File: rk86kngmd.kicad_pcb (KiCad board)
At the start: 2 copper layers, 226.2 x 62.5 mm, 39 parts, among them P1 GND, P10 TR00, P11 WPRT, P12 RD_DATA, P13 SIDE, P14 READY, P2 +5V, P3 IP, P4 DISC_A, P5 DISC_B, P6 DIR, P7 STEP, P8 WR_DATA, P9 WR_GATE, X1 ОНп-КС-23

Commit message: .
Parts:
- removed P1: GND, Pin_Headers:Pin_Header_Straight_1x01
- removed P10: TR00, Pin_Headers:Pin_Header_Straight_1x01
- removed P11: WPRT, Pin_Headers:Pin_Header_Straight_1x01
- removed P12: RD_DATA, Pin_Headers:Pin_Header_Straight_1x01
- removed P13: SIDE, Pin_Headers:Pin_Header_Straight_1x01
- removed P14: READY, Pin_Headers:Pin_Header_Straight_1x01
- removed P2: +5V, Pin_Headers:Pin_Header_Straight_1x01
- removed P3: IP, Pin_Headers:Pin_Header_Straight_1x01
- removed P4: DISC_A, Pin_Headers:Pin_Header_Straight_1x01
- removed P5: DISC_B, Pin_Headers:Pin_Header_Straight_1x01
- removed P6: DIR, Pin_Headers:Pin_Header_Straight_1x01
- removed P7: STEP, Pin_Headers:Pin_Header_Straight_1x01
- removed P8: WR_DATA, Pin_Headers:Pin_Header_Straight_1x01
- removed P9: WR_GATE, Pin_Headers:Pin_Header_Straight_1x01
- added C2: 0.1, Capacitor_THT:C_Disc_D6.0mm_W2.5mm_P5.00mm, F.Cu at (56.2, 106.2)
- added C3: 0.1, Capacitor_THT:C_Disc_D6.0mm_W2.5mm_P5.00mm, F.Cu at (96.8, 80.8)
- added D2: 2N4148, Diode_THT:D_A-405_P2.54mm_Vertical_AnodeUp, F.Cu at (53.5, 120.0)
- added DD1: К580ВВ55, rk86kngmd:DIP40-2.5mm, F.Cu at (86.5, 59.5)
- added J1: Conn_02x17_Odd_Even, Connector_IDC:IDC-Header_2x17_P2.54mm_Vertical, F.Cu at (46.4, 53.9)
- added J2: FD power, rk86kngmd:171826-4, F.Cu at (49.9, 104.7)
- added R8: 1K, Resistor_THT:R_Axial_DIN0207_L6.3mm_D2.5mm_P2.54mm_Vertical, F.Cu at (45.9, 117.4)
- C1: footprint Capacitors_ThroughHole:C_Disc_D6_P5 -> Capacitor_THT:C_Disc_D6.0mm_W2.5mm_P5.00mm
- D1: value К580ВВ55 -> 2N4148; footprint rk86kngmd:DIP40-2.5mm -> Diode_THT:D_A-405_P2.54mm_Vertical_AnodeUp
- DD10: value К555ИД4 -> 74LS155; footprint DIP16-2.5mm -> Package_SO:SOIC-16_3.9x9.9mm_P1.27mm; moved to B.Cu
- DD11, DD12: value К555ТМ2 -> 74LS74; footprint rk86ngmd:DIP14-2.5mm -> Package_SO:SOIC-14_3.9x8.7mm_P1.27mm
- DD13: value К555ЛА3 -> 74LS00; footprint rk86ngmd:DIP14-2.5mm -> Package_SO:SOIC-14_3.9x8.7mm_P1.27mm
- DD14: value К555ЛН1 -> 74LS04; footprint rk86ngmd:DIP14-2.5mm -> Package_SO:SOIC-14_3.9x8.7mm_P1.27mm
- DD15: value К555ЛИ1 -> 74LS08; footprint rk86ngmd:DIP14-2.5mm -> Package_SO:SOIC-14_3.9x8.7mm_P1.27mm
- DD16: value К555ЛЛ1 -> 74LS32; footprint rk86ngmd:DIP14-2.5mm -> Package_SO:SOIC-14_3.9x8.7mm_P1.27mm
- DD17: value К555ЛЕ1 -> 74LS02; footprint DIP14-2.5mm -> Package_SO:SOIC-14_3.9x8.7mm_P1.27mm
- DD2: value К555ИР13 -> К155ИР13; footprint DIP24-2.5mm -> rk86kngmd:DIP24-2.5mm
- DD3: value К555ИР23 -> 74LS374; footprint DIP20-2.5mm -> Package_SO:SOIC-20W_7.5x12.8mm_P1.27mm
- DD4: value 2716 -> 27C64; footprint rk86ngmd:DIP24-2.5mm -> Package_DIP:DIP-28_W15.24mm_Socket
- DD6: value К555ИР22 -> 74LS373; footprint rk86ngmd:DIP20-2.5mm -> Package_SO:SOIC-20W_7.5x12.8mm_P1.27mm
- DD7, DD8: value К555ИЕ5 -> 74LS93; footprint rk86ngmd:DIP14-2.5mm -> Package_SO:SOIC-14_3.9x8.7mm_P1.27mm; moved to B.Cu
- DD9: value К555ИЕ7 -> 74LS193; footprint rk86ngmd:DIP16-2.5mm -> Package_SO:SOIC-16_3.9x9.9mm_P1.27mm; moved to B.Cu
- R1, R2, R3, R4, R5, R7: footprint rk86ngmd:Resistor_Vertical_RM2_5mm -> Resistor_THT:R_Axial_DIN0207_L6.3mm_D2.5mm_P2.54mm_Vertical
- R6: footprint Resistor_Vertical_RM2_5mm -> Resistor_THT:R_Axial_DIN0207_L6.3mm_D2.5mm_P2.54mm_Vertical
- X1: footprint rk86ngmd:ОНп-КС-23 -> rk86kngmd:ОНп-КС-23
- moved DD7 153.7 mm to (112.0, 114.9), turned to 0 degrees
- moved DD8 152.6 mm to (112.4, 94.6), turned to 0 degrees
- moved DD13 132.9 mm to (108.3, 94.6), turned to 0 degrees
- moved DD9 122.3 mm to (120.3, 78.3), turned to 0 degrees
- moved DD15 121.2 mm to (123.1, 114.9), turned to 0 degrees
- moved DD10 114.0 mm to (104.7, 78.2), turned to 0 degrees
- moved DD14 111.8 mm to (105.8, 77.8), turned to 0 degrees
- moved DD2 105.8 mm to (61.6, 97.6), turned to 180 degrees
- moved R1 98.0 mm to (109.2, 104.7), turned to 0 degrees
- moved DD17 94.6 mm to (123.0, 77.6), turned to 0 degrees
- moved DD11 94.5 mm to (123.1, 94.6), turned to 0 degrees
- moved C1 85.8 mm to (118.9, 104.7), turned to 0 degrees
- moved DD12 81.9 mm to (123.1, 60.0), turned to 0 degrees
- moved D1 72.1 mm to (49.9, 120.0), turned to 90 degrees
- moved DD3 58.0 mm to (85.5, 78.3)
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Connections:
- D1 pad 1: Net-(D1-Pad1) -> /CS1
- D1 pad 2: Net-(D1-Pad2) -> /CS12
- DD16 pad 8: Net-(D1-Pad6) -> Net-(DD1-Pad6)
- DD2 pad 15: Net-(D1-Pad40) -> Net-(DD1-Pad40)
- DD2 pad 17: Net-(D1-Pad39) -> Net-(DD1-Pad39)
- DD2 pad 19: Net-(D1-Pad38) -> Net-(DD1-Pad38)
- DD2 pad 21: Net-(D1-Pad37) -> Net-(DD1-Pad37)
- DD2 pad 3: Net-(D1-Pad4) -> Net-(DD1-Pad4)
- DD2 pad 5: Net-(D1-Pad3) -> Net-(DD1-Pad3)
- DD2 pad 7: Net-(D1-Pad2) -> Net-(DD1-Pad2)
- DD2 pad 9: Net-(D1-Pad1) -> Net-(DD1-Pad1)
- DD4 pad 1: /A7 -> +5V
- DD4 pad 10: /D1 -> /A0
- DD4 pad 11: /D2 -> /D0
- DD4 pad 12: GND -> /D1
- DD4 pad 13: /D3 -> /D2
- DD4 pad 14: /D4 -> GND
- DD4 pad 15: /D5 -> /D3
- DD4 pad 16: /D6 -> /D4
- DD4 pad 17: /D7 -> /D5
- DD4 pad 18: /CS1 -> /D6
- DD4 pad 19: /A10 -> /D7
- DD4 pad 2: /A6 -> GND
- DD4 pad 20: /RD -> /CS12
- DD4 pad 21: +5V -> /A10
- DD4 pad 22: /A9 -> /RD
- DD4 pad 23: /A8 -> /A11
- DD4 pad 24: +5V -> /A9
- DD4 pad 3: /A5 -> /A7
- DD4 pad 4: /A4 -> /A6
- DD4 pad 5: /A3 -> /A5
- DD4 pad 6: /A2 -> /A4
- DD4 pad 7: /A1 -> /A3
- DD4 pad 8: /A0 -> /A2
- DD4 pad 9: /D0 -> /A1
- X1 pad B11: Net-(X1-PadB11) -> +12V
- X1 pad B23: Net-(X1-PadB23) -> /A11
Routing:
- net GND: track 608.9 -> 0.00 mm, vias 10 -> 0
- net +5V: track 574.7 -> 0.00 mm, vias 6 -> 0
- net Net-(DD10-Pad1): track 372.7 -> 0.00 mm, vias 16 -> 0
- net Net-(DD15-Pad11): track 247.4 -> 0.00 mm, vias 8 -> 0
- net RD_DATA: track 247.0 -> 0.00 mm, vias 13 -> 0
- net /RD: track 238.5 -> 0.00 mm, vias 8 -> 0
- net /WRDATA: track 219.4 -> 0.00 mm, vias 8 -> 0
- net /OSC: track 218.3 -> 0.00 mm, vias 4 -> 0
- net /WRGATE: track 202.8 -> 0.00 mm, vias 9 -> 0
- net Net-(DD12-Pad13): track 200.3 -> 0.00 mm, vias 3 -> 0
- net Net-(DD16-Pad3): track 175.5 -> 0.00 mm, vias 5 -> 0
- net /A2: track 175.1 -> 0.00 mm, vias 4 -> 0
- net /WR: track 169.8 -> 0.00 mm, vias 5 -> 0
- net Net-(DD11-Pad3): track 159.7 -> 0.00 mm, vias 5 -> 0
- net /D4: track 146.2 -> 0.00 mm, vias 6 -> 0
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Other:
- board size 226.2 x 62.5 mm -> 86.9 x 84.7 mm
- board text added: "+12"
- board text added: "+5"
- board text added: "Gnd"
- board text added: "RK86 FD Controller"
- board text added: "©2020 SDS"
- board text removed: "2016 tnt23"

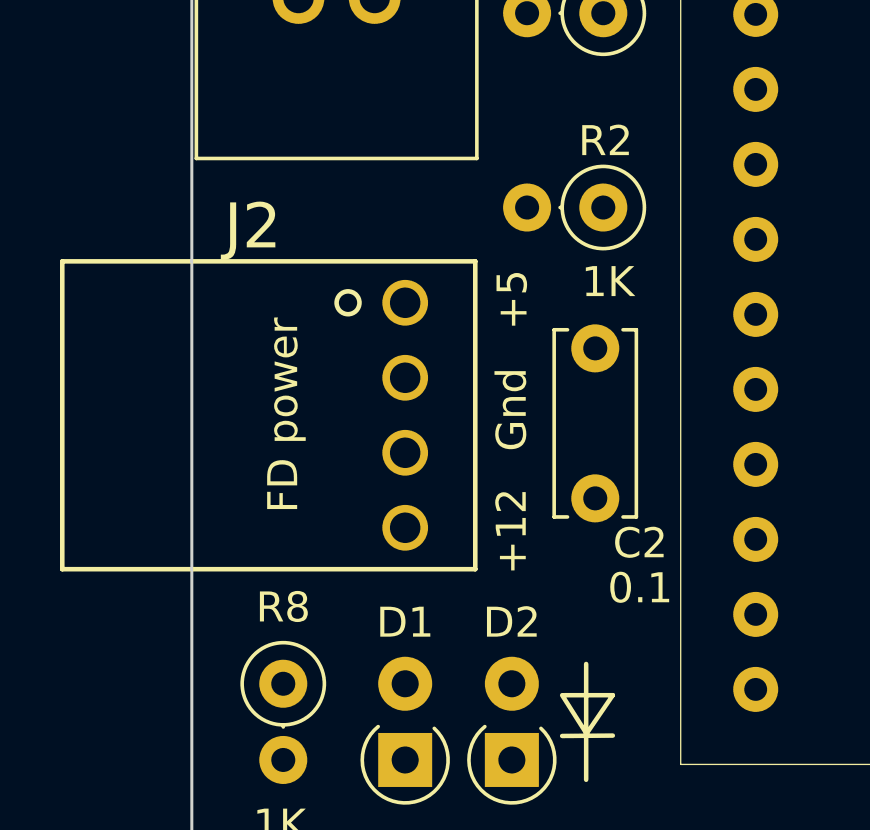
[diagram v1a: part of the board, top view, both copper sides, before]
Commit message: Updated libraries
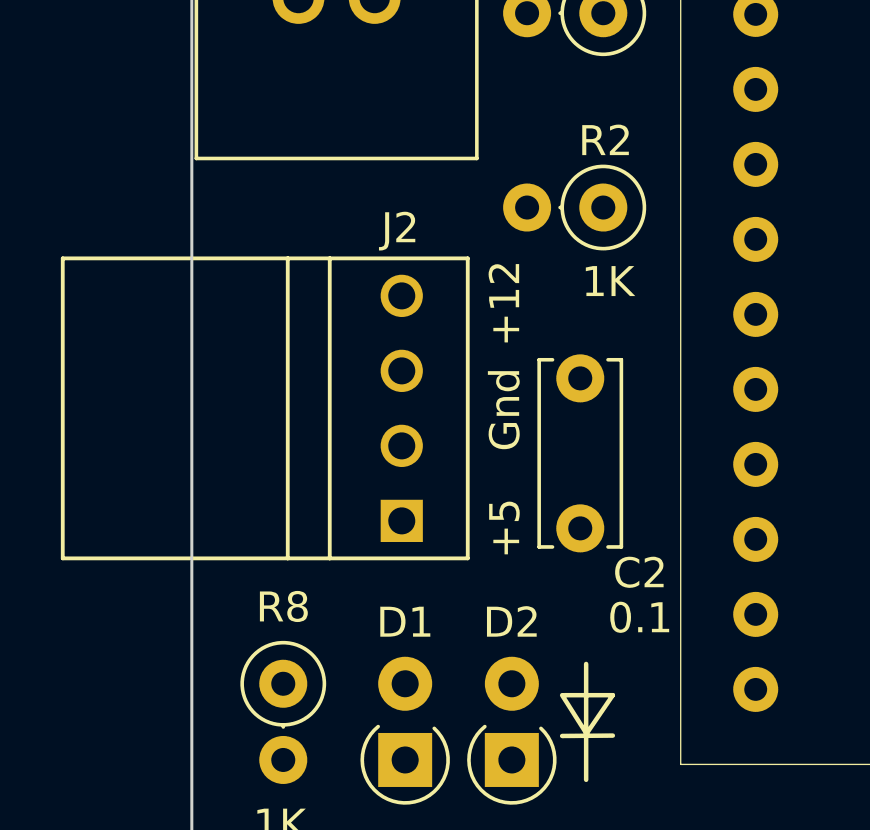
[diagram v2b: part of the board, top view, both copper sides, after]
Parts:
- J2: footprint rk86kngmd:171826-4 -> rk86kngmd:TE_171826-4
- moved C2 6.02 mm to (55.8, 112.2), turned to 90 degrees
- moved J2 5.84 mm to (45.2, 108.2)
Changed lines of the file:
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@@
     (add_net GND)
+  )
+  (module rk86kngmd:TE_171826-4 (layer F.Cu)
+    (at 45.25 108.25 270)
+    (fp_text reference J2 (at -6 -4.5 180) (layer F.SilkS)
+      (effects (font (size 1 1) (thickness 0.15)))
+    )
+    (fp_text value "FD power" (at 1.991485 7.991205 90) (layer F.Fab)
+      (effects (font (size 1.003283 1.003283) (thickness 0.015)))
+    )
+    (fp_line (start -5 -2.15) (end 5 -2.15) (layer F.SilkS) (width 0.127))
+    (fp_line (start -5 -0.75) (end 5 -0.75) (layer F.SilkS) (width 0.127))
+    (fp_line (start 5 6.75) (end -5 6.75) (layer F.Fab) (width 0.127))
+    (fp_line (start -5 -6.75) (end 5 -6.75) (layer F.Fab) (width 0.127))
+    (fp_line (start -5 6.75) (end -5 -6.75) (layer F.Fab) (width 0.127))
+    (fp_line (start 5 6.75) (end 5 -6.75) (layer F.Fab) (width 0.127))
+    (fp_line (start -5.25 7) (end -5.25 -7) (layer F.CrtYd) (width 0.05))
+    (fp_line (start 5.25 7) (end -5.25 7) (layer F.CrtYd) (width 0.05))
+    (fp_line (start 5.25 -7) (end 5.25 7) (layer F.CrtYd) (width 0.05))
+    (fp_line (start -5.25 -7) (end 5.25 -7) (layer F.CrtYd) (width 0.05))
+    (fp_line (start -5 -2.15) (end -5 -6.75) (layer F.SilkS) (width 0.127))
+    (fp_line (start -5 -0.75) (end -5 -2.15) (layer F.SilkS) (width 0.127))
+    (fp_line (start -5 6.75) (end -5 -0.75) (layer F.SilkS) (width 0.127))
+    (fp_line (start 5 6.75) (end -5 6.75) (layer F.SilkS) (width 0.127))
+    (fp_line (start 5 -0.75) (end 5 6.75) (layer F.SilkS) (width 0.127))
+    (fp_line (start 5 -2.15) (end 5 -0.75) (layer F.SilkS) (width 0.127))
+    (fp_line (start 5 -6.75) (end 5 -2.15) (layer F.SilkS) (width 0.127))
+    (fp_line (start -5 -6.75) (end 5 -6.75) (layer F.SilkS) (width 0.127))
+    (pad 1 thru_hole rect (at 3.75 -4.55 270) (size 1.408 1.408) (drill 0.9) (layers *.Cu *.Mask)
+      (net 21 +5V))
+    (pad 2 thru_hole circle (at 1.25 -4.55 270) (size 1.408 1.408) (drill 0.9) (layers *.Cu *.Mask)
+      (net 1 GND))
+    (pad 3 thru_hole circle (at -1.25 -4.55 270) (size 1.408 1.408) (drill 0.9) (layers *.Cu *.Mask)
+      (net 1 GND))
+    (pad 4 thru_hole circle (at -3.75 -4.55 270) (size 1.408 1.408) (drill 0.9) (layers *.Cu *.Mask)
+      (net 163 +12V))
   )
   (module Capacitor_THT:C_Disc_D6.0mm_W2.5mm_P5.00mm (layer F.Cu)
@@
   )
   (module Capacitor_THT:C_Disc_D6.0mm_W2.5mm_P5.00mm (layer F.Cu)
-    (at 56.25 106.25 270)
+    (at 55.75 112.25 90)
     (descr "C, Disc series, Radial, pin pitch=5.00mm, , diameter*width=6*2.5mm^2, Capacitor, http://cdn-reichelt.de/documents/datenblatt/B300/DS_KERKO_TC.pdf")
     (tags "C Disc series Radial pin pitch 5.00mm  diameter 6mm width 2.5mm Capacitor")
-    (fp_text reference C2 (at 6.5 -1.5 180) (layer F.SilkS)
-      (effects (font (size 1 1) (thickness 0.15)))
-    )
-    (fp_text value 0.1 (at 8 -1.5) (layer F.SilkS)
+    (fp_text reference C2 (at -1.5 2 180) (layer F.SilkS)
+      (effects (font (size 1 1) (thickness 0.15)))
+    )
+    (fp_text value 0.1 (at -3 2) (layer F.SilkS)
       (effects (font (size 1 1) (thickness 0.15)))
     )
@@
     (fp_line (start -0.5 1.25) (end 5.5 1.25) (layer F.Fab) (width 0.1))
     (fp_line (start -0.5 -1.25) (end -0.5 1.25) (layer F.Fab) (width 0.1))
-    (pad 2 thru_hole circle (at 5 0 270) (size 1.6 1.6) (drill 0.8) (layers *.Cu *.Mask)
-      (net 1 GND))
-    (pad 1 thru_hole circle (at 0 0 270) (size 1.6 1.6) (drill 0.8) (layers *.Cu *.Mask)
+    (pad 2 thru_hole circle (at 5 0 90) (size 1.6 1.6) (drill 0.8) (layers *.Cu *.Mask)
+      (net 1 GND))
+    (pad 1 thru_hole circle (at 0 0 90) (size 1.6 1.6) (drill 0.8) (layers *.Cu *.Mask)
       (net 21 +5V))
     (model ${KISYS3DMOD}/Capacitor_THT.3dshapes/C_Disc_D6.0mm_W2.5mm_P5.00mm.wrl
@@
       (rotate (xyz 0 0 0))
     )
-  )
-  (module rk86kngmd:171826-4 (layer F.Cu)
-    (at 49.914 104.73 270)
-    (fp_text reference J2 (at -2.54 5.08 180) (layer F.SilkS)
-      (effects (font (size 1.5 1.5) (thickness 0.15)))
-    )
-    (fp_text value "FD power" (at 3.75 4.064 90) (layer F.SilkS)
-      (effects (font (size 1 1) (thickness 0.15)))
-    )
-    (fp_circle (center 0 1.905) (end 0.381 1.905) (layer F.Fab) (width 0.1524))
-    (fp_circle (center 0 1.905) (end 0.381 1.905) (layer B.SilkS) (width 0.1524))
-    (fp_circle (center 0 1.905) (end 0.381 1.905) (layer F.SilkS) (width 0.1524))
-    (fp_line (start 9.0078 -2.4638) (end -1.5078 -2.4638) (layer F.CrtYd) (width 0.1524))
-    (fp_line (start 9.0078 11.557) (end 9.0078 -2.4638) (layer F.CrtYd) (width 0.1524))
-    (fp_line (start -1.5078 11.557) (end 9.0078 11.557) (layer F.CrtYd) (width 0.1524))
-    (fp_line (start -1.5078 -2.4638) (end -1.5078 11.557) (layer F.CrtYd) (width 0.1524))
-    (fp_line (start -1.2538 -2.2098) (end -1.2538 11.303) (layer F.Fab) (width 0.1524))
-    (fp_line (start 8.7538 -2.2098) (end -1.2538 -2.2098) (layer F.Fab) (width 0.1524))
-    (fp_line (start 8.7538 11.303) (end 8.7538 -2.2098) (layer F.Fab) (width 0.1524))
-    (fp_line (start -1.2538 11.303) (end 8.7538 11.303) (layer F.Fab) (width 0.1524))
-    (fp_line (start -1.3808 -2.3368) (end -1.3808 11.43) (layer F.SilkS) (width 0.1524))
-    (fp_line (start 8.8808 -2.3368) (end -1.3808 -2.3368) (layer F.SilkS) (width 0.1524))
-    (fp_line (start 8.8808 11.43) (end 8.8808 -2.3368) (layer F.SilkS) (width 0.1524))
-    (fp_line (start -1.3808 11.43) (end 8.8808 11.43) (layer F.SilkS) (width 0.1524))
-    (fp_text user "Copyright 2016 Accelerated Designs. All rights reserved." (at 0 0 90) (layer Cmts.User)
-      (effects (font (size 0.127 0.127) (thickness 0.002)))
-    )
-    (pad 4 thru_hole circle (at 7.5 0 270) (size 1.524 1.524) (drill 1.016) (layers *.Cu *.Mask)
-      (net 163 +12V))
-    (pad 3 thru_hole circle (at 5 0 270) (size 1.524 1.524) (drill 1.016) (layers *.Cu *.Mask)
-      (net 1 GND))
-    (pad 2 thru_hole circle (at 2.5 0 270) (size 1.524 1.524) (drill 1.016) (layers *.Cu *.Mask)
-      (net 1 GND))
-    (pad 1 thru_hole circle (at 0 0 270) (size 1.524 1.524) (drill 1.016) (layers *.Cu *.Mask)
-      (net 21 +5V))
   )
   (module rk86kngmd:ОНп-КС-23 (layer F.Cu)
@@
     (effects (font (size 2 2) (thickness 0.3)) (justify mirror))
   )
-  (gr_text Gnd (at 53.47 108.286 90) (layer F.SilkS)
+  (gr_text Gnd (at 53.25 108.286 90) (layer F.SilkS)
     (effects (font (size 1 1) (thickness 0.15)))
   )
-  (gr_text +5 (at 53.4954 104.6284 90) (layer F.SilkS)
+  (gr_text +5 (at 53.25 112.25 90) (layer F.SilkS)
     (effects (font (size 1 1) (thickness 0.15)))
   )
-  (gr_text +12 (at 53.47 112.35 90) (layer F.SilkS)
+  (gr_text +12 (at 53.25 104.75 90) (layer F.SilkS)
     (effects (font (size 1 1) (thickness 0.15)))
   )

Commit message: board routed
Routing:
- net GND: track 0.00 -> 498.6 mm, vias 0 -> 4
- net +5V: track 0.00 -> 427.5 mm, vias 0 -> 5
- net Net-(DD10-Pad1): track 0.00 -> 231.3 mm, vias 0 -> 3
- net /WR: track 0.00 -> 145.1 mm, vias 0 -> 1
- net /RD: track 0.00 -> 118.1 mm, vias 0 -> 3
- net /D2: track 0.00 -> 117.9 mm, vias 0 -> 1
- net /D1: track 0.00 -> 116.4 mm, vias 0 -> 1
- net Net-(DD13-Pad1): track 0.00 -> 114.1 mm, vias 0 -> 3
- net /D0: track 0.00 -> 109.6 mm, vias 0 -> 3
- net Net-(DD11-Pad3): track 0.00 -> 108.8 mm, vias 0 -> 6
- net Net-(DD17-Pad1): track 0.00 -> 105.4 mm, vias 0 -> 1
- net TR00: track 0.00 -> 103.7 mm
- net READY: track 0.00 -> 103.5 mm
- net /D7: track 0.00 -> 102.0 mm, vias 0 -> 1
- net Net-(DD12-Pad5): track 0.00 -> 101.1 mm, vias 0 -> 1
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- added copper zone on B.Cu, net GND
- added copper zone on F.Cu, net GND

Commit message: Switched to SMD components
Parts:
- C1: footprint Capacitor_THT:C_Disc_D6.0mm_W2.5mm_P5.00mm -> Capacitor_SMD:C_1206_3216Metric_Pad1.42x1.75mm_HandSolder
- C2, C3: value 0.1 -> 0μ1; footprint Capacitor_THT:C_Disc_D6.0mm_W2.5mm_P5.00mm -> Capacitor_SMD:C_1206_3216Metric_Pad1.42x1.75mm_HandSolder
- D1, D2: footprint Diode_THT:D_A-405_P2.54mm_Vertical_AnodeUp -> Diode_SMD:D_1206_3216Metric_Pad1.42x1.75mm_HandSolder
- R1, R2, R3, R4, R5, R6, R7, R8: footprint Resistor_THT:R_Axial_DIN0207_L6.3mm_D2.5mm_P2.54mm_Vertical -> Resistor_SMD:R_1206_3216Metric_Pad1.42x1.75mm_HandSolder
- moved R2 2.43 mm to (55.8, 99.2)
- moved C3 1.71 mm to (97.0, 79.0)
- moved D1 1.49 mm to (49.8, 118.5)
- moved D2 1.48 mm to (53.5, 118.5)
- moved C2 1.20 mm to (55.8, 111.0)
- moved R8 1.07 mm to (46.0, 118.5)
- moved R4 0.81 mm to (55.8, 82.9)
- moved R6 0.81 mm to (55.8, 87.0)
- moved R5 0.77 mm to (55.8, 95.1)
- moved R7 0.77 mm to (55.8, 91.0)
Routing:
- net RD_DATA: track 89.0 -> 163.3 mm, vias 0 -> 1
- net Net-(DD11-Pad10): track 91.1 -> 49.7 mm, vias 2 -> 0
- net +5V: track 427.5 -> 466.5 mm, vias 5 -> 9
- net Net-(DD13-Pad1): track 114.1 -> 138.6 mm, vias 3 -> 2
- net /D2: track 117.9 -> 142.4 mm
- net DISC_A: track 53.2 -> 29.1 mm, vias 1 -> 0
- net Net-(DD11-Pad11): track 71.2 -> 47.5 mm, vias 2 -> 3
- net Net-(DD15-Pad11): track 35.6 -> 59.3 mm, vias 2 -> 0
- net /WRGATE: track 88.1 -> 106.2 mm
- net GND: track 498.6 -> 481.3 mm, vias 4 -> 24
- net DISC_B: track 48.1 -> 31.4 mm
- net /RD: track 118.1 -> 134.3 mm, vias 3 -> 1
- net /D1: track 116.4 -> 100.5 mm, vias 1 -> 2
- net /PC4: track 60.7 -> 46.6 mm
- net Net-(DD10-Pad1): track 231.3 -> 245.0 mm, vias 3 -> 4
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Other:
- outline, holes or cut-outs redrawn
- board text added: "RK86-FD Controller"
- board text removed: "RK86 FD Controller"
